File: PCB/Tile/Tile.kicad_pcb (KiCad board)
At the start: 2 copper layers, 100 x 86.6 mm, 40 parts, among them J1 Conn_01x05_Male, U1 HT16K33-28SOP

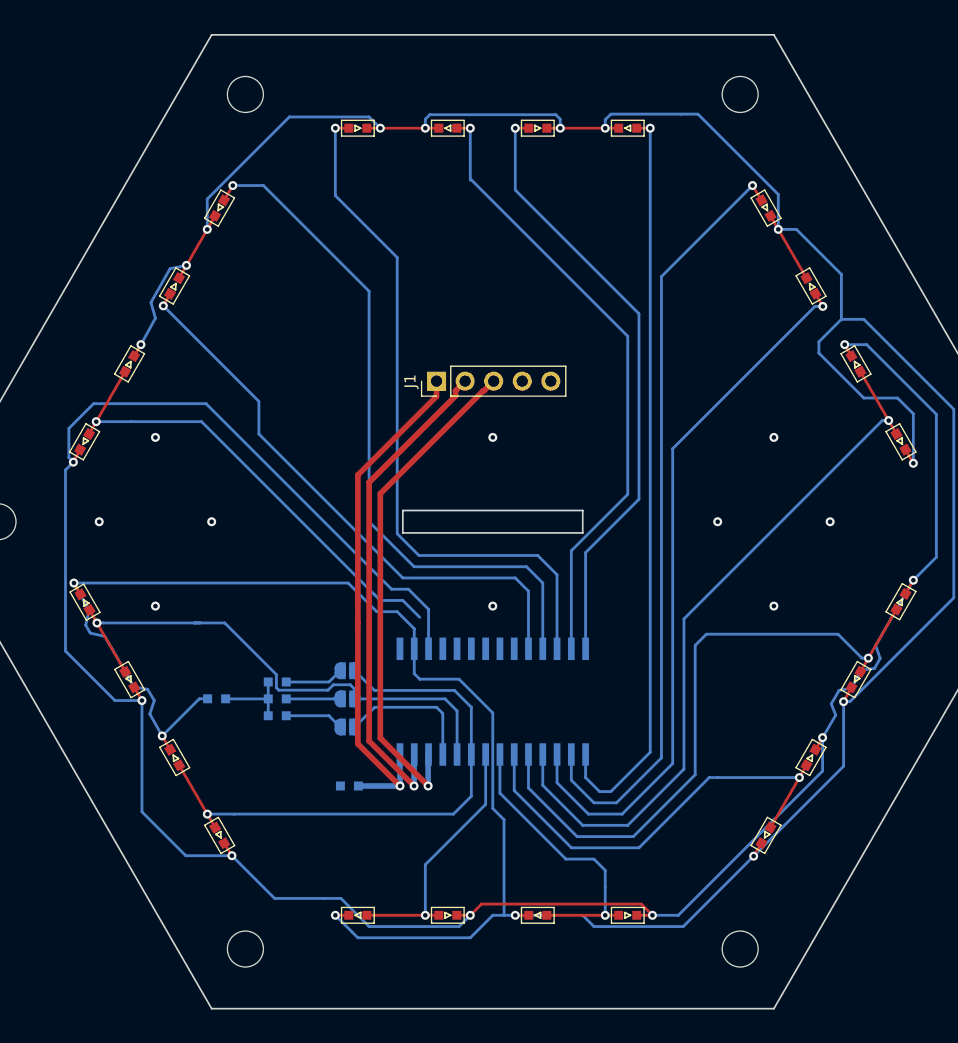
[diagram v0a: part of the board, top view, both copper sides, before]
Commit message: [update] TileのIC位置を移動 #3
* ICを手前の裏に配置すると表面に配線やビアが
  見えてしまうので奥側に移動
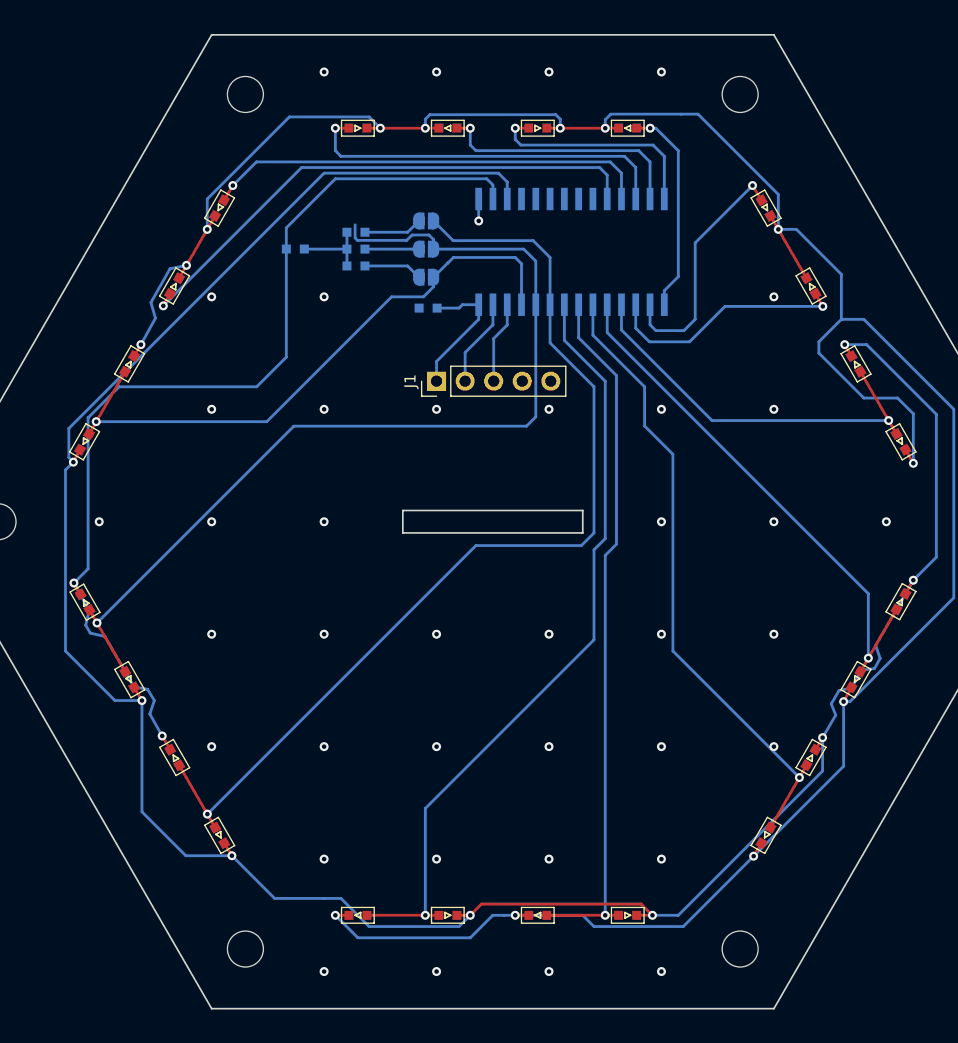
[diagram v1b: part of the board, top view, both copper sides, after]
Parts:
- moved C1 43.1 mm to (124.2, 86.0)
- moved D26 40.6 mm to (112.4, 80.7)
- moved JP1 40.6 mm to (124.1, 83.3)
- moved JP2 40.6 mm to (124.1, 80.8)
- moved JP3 40.6 mm to (124.1, 78.3)
- moved R1 40.6 mm to (117.8, 82.3)
- moved R2 40.6 mm to (117.8, 80.8)
- moved R3 40.6 mm to (117.8, 79.3)
- moved U1 40.6 mm to (137.0, 81.0)
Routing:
- net Net-(D11-Pad2): track 66.5 -> 18.7 mm
- net Net-(D10-Pad2): track 68.6 -> 22.0 mm
- net Net-(D20-Pad2): track 22.9 -> 68.8 mm
- net Net-(D9-Pad2): track 63.7 -> 21.8 mm
- net Net-(D19-Pad2): track 50.2 -> 89.0 mm
- net Net-(D18-Pad2): track 47.6 -> 85.8 mm
- net SCL: track 44.8 -> 7.35 mm, vias 1 -> 0
- net Net-(D21-Pad2): track 26.0 -> 62.5 mm
- net SDA: track 44.0 -> 7.86 mm, vias 1 -> 0
- net +5V: track 47.0 -> 12.2 mm, vias 1 -> 0
- net Net-(D12-Pad2): track 54.0 -> 19.9 mm
- net Net-(D13-Pad2): track 55.4 -> 22.6 mm
- net Net-(D14-Pad2): track 61.9 -> 33.3 mm
- net Net-(D24-Pad2): track 64.1 -> 35.7 mm
- net Net-(D15-Pad2): track 61.6 -> 39.7 mm
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
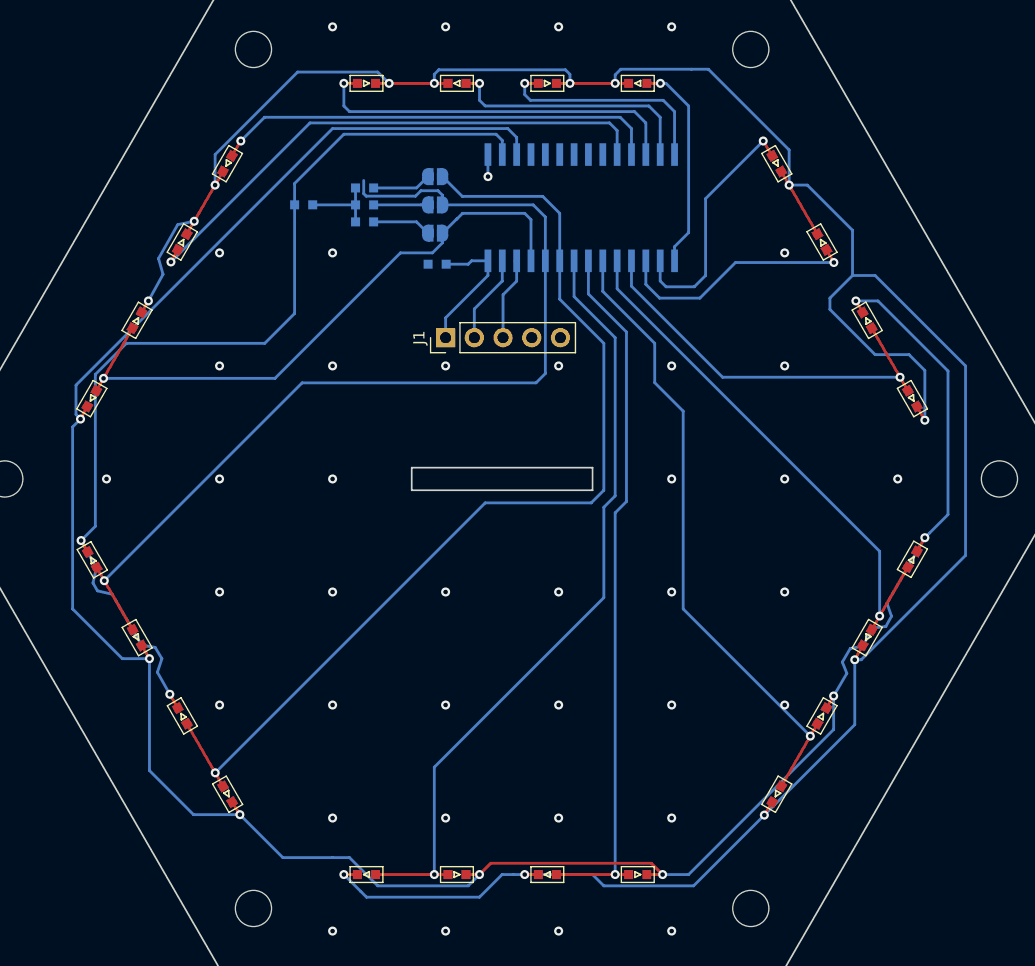
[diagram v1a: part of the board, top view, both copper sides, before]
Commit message: [update] Tileの配線改善(裏面外周) #3
* 裏面外周の配線を60度に沿うように修正
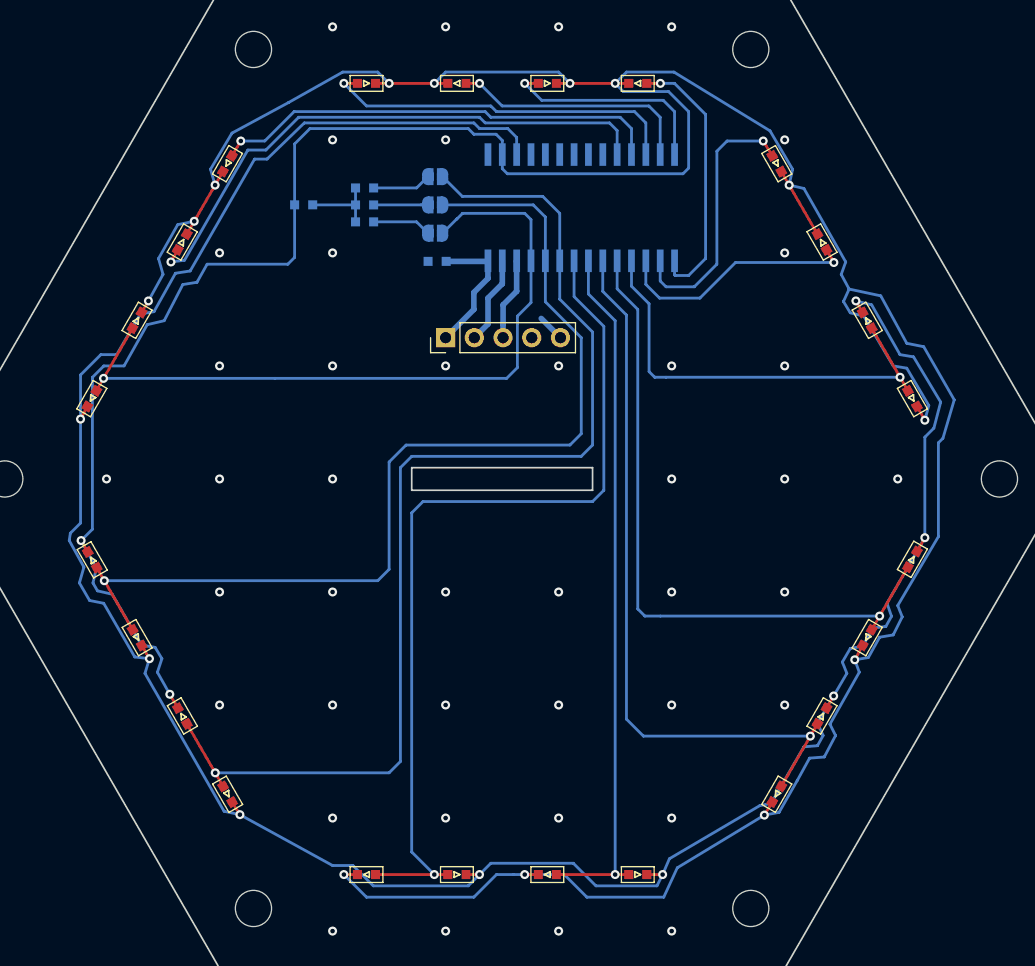
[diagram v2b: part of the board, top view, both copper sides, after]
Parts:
- moved C1 0.25 mm to (124.2, 85.8)
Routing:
- net Net-(D1-Pad1): track 321.3 -> 345.4 mm
- net Net-(D23-Pad2): track 47.5 -> 59.6 mm
- net Net-(D19-Pad2): track 89.0 -> 100.4 mm
- net Net-(D1-Pad2): track 54.6 -> 65.9 mm
- net Net-(D20-Pad2): track 68.8 -> 78.4 mm
- net Net-(D22-Pad2): track 56.1 -> 64.7 mm
- net Net-(D11-Pad2): track 18.7 -> 23.7 mm
- net Net-(D18-Pad2): track 85.8 -> 89.5 mm
- net Net-(D24-Pad2): track 35.7 -> 39.3 mm
- net Net-(D16-Pad2): track 48.2 -> 50.2 mm
- net Net-(D10-Pad2): track 22.0 -> 23.9 mm
- net Net-(D14-Pad2): track 33.3 -> 32.2 mm
- net Net-(D17-Pad1): track 217.8 -> 216.8 mm
- net Net-(D13-Pad2): track 22.6 -> 21.7 mm
- net Net-(D21-Pad2): track 62.5 -> 61.7 mm
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
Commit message: [add] Tileにロゴマークを追加 #3
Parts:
- added G***: LOGO, logos:logo_750dpi, F.Cu at (130.0, 122.0)
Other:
- board text added: "@ext_sui 2020.05"
- board text removed: "@ext_sui 2020.04"

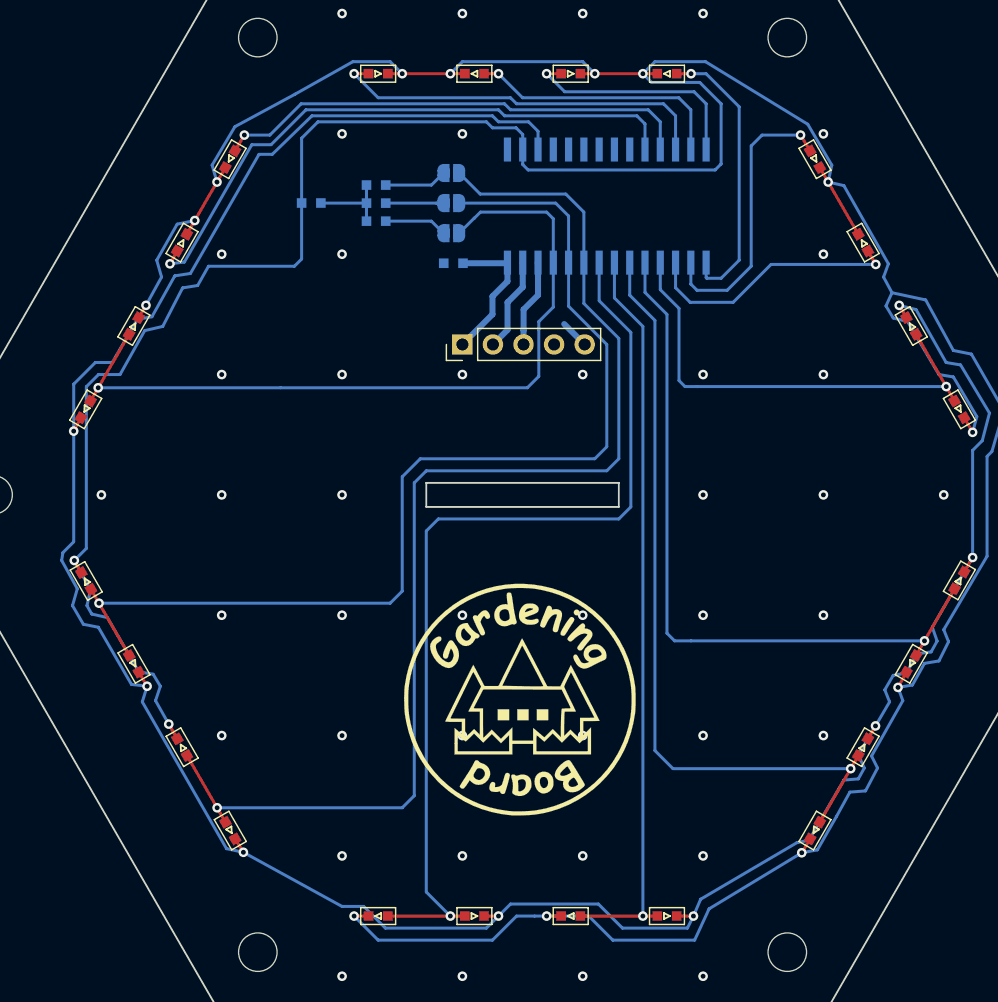
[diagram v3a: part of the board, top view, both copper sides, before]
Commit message: [update] Tileの配線改善(GNDビア, 配線全体) #3
* GNDビアを等間隔に空けるためにIC位置をさらにずらした
* 基板下から中央への配線のY座標を左右で統一
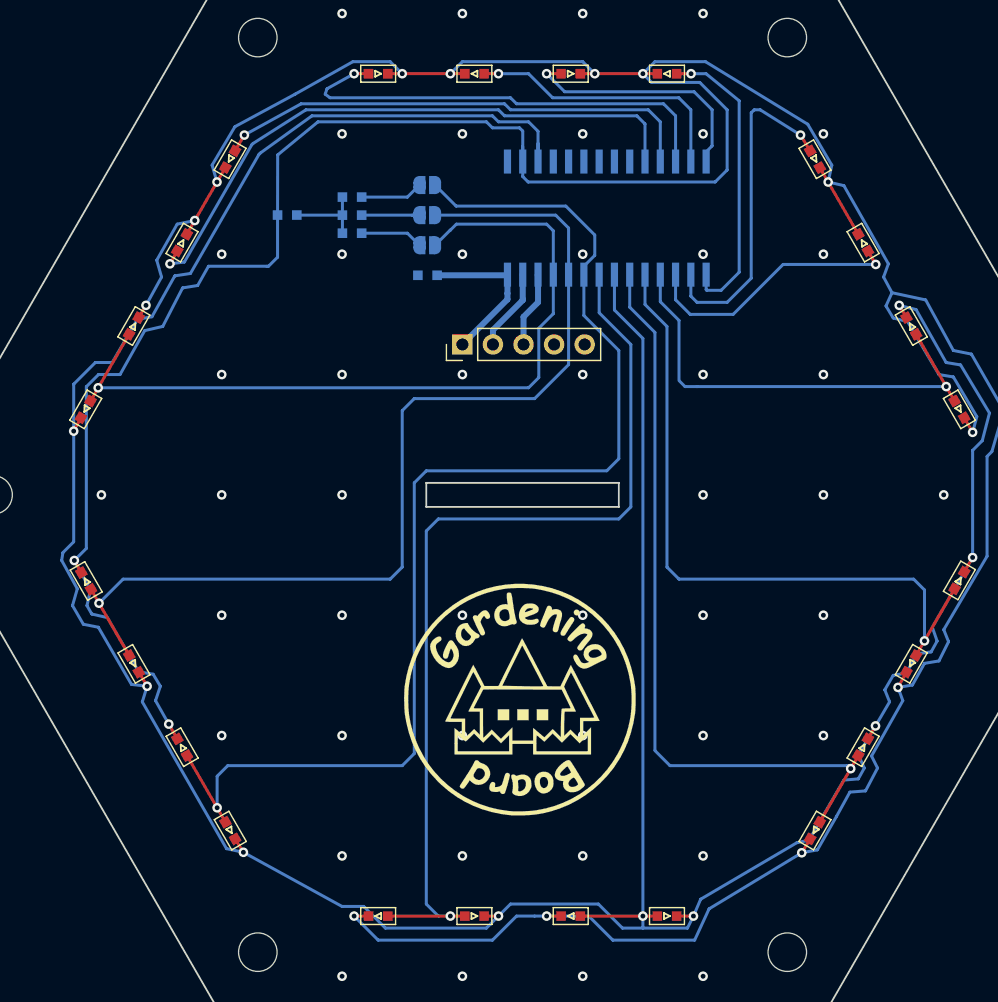
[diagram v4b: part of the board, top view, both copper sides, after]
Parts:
- moved C1 2.37 mm to (122.1, 86.8)
- moved D26 2.24 mm to (110.4, 81.7)
- moved JP1 2.24 mm to (122.1, 84.3)
- moved JP2 2.24 mm to (122.1, 81.8)
- moved JP3 2.24 mm to (122.1, 79.3)
- moved R1 2.24 mm to (115.8, 83.3)
- moved R2 2.24 mm to (115.8, 81.8)
- moved R3 2.24 mm to (115.8, 80.3)
- moved U1 1.00 mm to (137.0, 82.0)
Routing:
- net Net-(D14-Pad2): track 32.2 -> 37.9 mm
- net Net-(D18-Pad2): track 89.5 -> 84.1 mm
- net Net-(D10-Pad2): track 23.9 -> 27.9 mm
- net Net-(D1-Pad1): track 345.4 -> 348.2 mm
- net GND: track 2.40 -> 0.00 mm, vias 42 -> 47
- net Net-(D17-Pad1): track 216.8 -> 219.1 mm
- net Net-(D23-Pad2): track 59.6 -> 57.9 mm
- net Net-(D12-Pad2): track 19.3 -> 20.7 mm
- net Net-(D19-Pad2): track 100.4 -> 101.7 mm
- net Net-(D11-Pad2): track 23.7 -> 24.9 mm
- net +5V: track 12.1 -> 13.2 mm
- net Net-(D24-Pad2): track 39.3 -> 38.2 mm
- net Net-(D22-Pad2): track 64.7 -> 63.7 mm
- net SCL: track 7.35 -> 6.35 mm
- net SDA: track 7.85 -> 6.85 mm
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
